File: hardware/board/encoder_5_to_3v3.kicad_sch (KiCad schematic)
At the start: 6 parts, among them U1 74LVCH2T45DC

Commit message: update schematic
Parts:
- renumbered C39 to C26, C19 to C27, C19 to C3, C9 to C4, U1 to U?
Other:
- note added: "B set to input."
- note added: "External Encoder Input"
- note removed: "Encoder Input"
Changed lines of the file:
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@@
     (stroke (width 0) (type default))
   )
-  (text "Encoder\nInput" (at 170.815 95.25 0)
+  (text "External\nEncoder\nInput" (at 170.815 97.155 0)
+    (effects (font (size 1.27 1.27)) (justify left bottom))
+  )
+  (text "B set to input." (at 116.84 103.505 0)
     (effects (font (size 1.27 1.27)) (justify left bottom))
   )
@@
   (symbol (lib_id "power:GND") (at 144.145 109.22 0) (unit 1)
     (in_bom yes) (on_board yes) (dnp no) (fields_autoplaced)
-    (property "Reference" "#PWR099" (at 144.145 115.57 0)
+    (property "Reference" "#PWR091" (at 144.145 115.57 0)
       (effects (font (size 1.27 1.27)) hide)
     )
@@
   (symbol (lib_id "Device:C") (at 168.275 182.245 180) (unit 1)
     (in_bom yes) (on_board yes) (dnp no)
-    (property "Reference" "C19" (at 172.085 179.705 0)
+    (property "Reference" "C27" (at 172.085 179.705 0)
       (effects (font (size 1.27 1.27)) (justify left))
     )
@@
   (symbol (lib_id "power:+5V") (at 168.275 177.165 0) (unit 1)
     (in_bom yes) (on_board yes) (dnp no)
-    (property "Reference" "#PWR0115" (at 168.275 180.975 0)
+    (property "Reference" "#PWR097" (at 168.275 180.975 0)
       (effects (font (size 1.27 1.27)) hide)
     )
@@
   (symbol (lib_id "Device:C") (at 136.525 182.245 180) (unit 1)
     (in_bom yes) (on_board yes) (dnp no)
-    (property "Reference" "C19" (at 140.335 179.705 0)
+    (property "Reference" "C3" (at 140.335 179.705 0)
       (effects (font (size 1.27 1.27)) (justify left))
     )
@@
   (symbol (lib_id "power:GND") (at 158.115 187.325 0) (unit 1)
     (in_bom yes) (on_board yes) (dnp no)
-    (property "Reference" "#PWR083" (at 158.115 193.675 0)
+    (property "Reference" "#PWR096" (at 158.115 193.675 0)
       (effects (font (size 1.27 1.27)) hide)
     )
@@
   (symbol (lib_id "power:GND") (at 168.275 187.325 0) (unit 1)
     (in_bom yes) (on_board yes) (dnp no)
-    (property "Reference" "#PWR0114" (at 168.275 193.675 0)
+    (property "Reference" "#PWR098" (at 168.275 193.675 0)
       (effects (font (size 1.27 1.27)) hide)
     )
@@
   (symbol (lib_id "Device:C") (at 144.78 182.245 0) (unit 1)
     (in_bom yes) (on_board yes) (dnp no)
-    (property "Reference" "C9" (at 146.05 179.705 0)
+    (property "Reference" "C4" (at 146.05 179.705 0)
       (effects (font (size 1.27 1.27)) (justify left))
     )
@@
   (symbol (lib_id "Logic_LevelTranslator:74LVCH2T45DC") (at 144.145 94.615 0) (unit 1)
     (in_bom yes) (on_board yes) (dnp no) (fields_autoplaced)
-    (property "Reference" "U1" (at 146.3391 106.68 0)
+    (property "Reference" "U?" (at 146.3391 106.68 0)
       (effects (font (size 1.27 1.27)) (justify left))
     )
@@
   (symbol (lib_id "power:GND") (at 144.78 187.325 0) (unit 1)
     (in_bom yes) (on_board yes) (dnp no)
-    (property "Reference" "#PWR081" (at 144.78 193.675 0)
+    (property "Reference" "#PWR093" (at 144.78 193.675 0)
       (effects (font (size 1.27 1.27)) hide)
     )
@@
   (symbol (lib_id "power:GND") (at 136.525 187.325 0) (unit 1)
     (in_bom yes) (on_board yes) (dnp no)
-    (property "Reference" "#PWR0113" (at 136.525 193.675 0)
+    (property "Reference" "#PWR089" (at 136.525 193.675 0)
       (effects (font (size 1.27 1.27)) hide)
     )
@@
   (symbol (lib_id "power:+5V") (at 158.115 177.165 0) (unit 1)
     (in_bom yes) (on_board yes) (dnp no)
-    (property "Reference" "#PWR082" (at 158.115 180.975 0)
+    (property "Reference" "#PWR095" (at 158.115 180.975 0)
       (effects (font (size 1.27 1.27)) hide)
     )
@@
   (symbol (lib_id "power:GND") (at 161.925 99.695 0) (unit 1)
     (in_bom yes) (on_board yes) (dnp no)
-    (property "Reference" "#PWR099" (at 161.925 106.045 0)
+    (property "Reference" "#PWR0100" (at 161.925 106.045 0)
       (effects (font (size 1.27 1.27)) hide)
     )
@@
   (symbol (lib_id "Device:C") (at 158.115 182.245 0) (unit 1)
     (in_bom yes) (on_board yes) (dnp no)
-    (property "Reference" "C39" (at 159.385 179.705 0)
-      (effects (font (size 1.27 1.27)) (justify left))
-    )
+    (property "Reference" "C26" (at 159.385 179.705 0)
+      (effects (font (size 1.27 1.27)) (justify left))
+    )

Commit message: update schematic
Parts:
- added C33: 1uF, Capacitor_SMD:C_0402_1005Metric, symbol Device:C
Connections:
- net +5V: now also C33.1
- net GND: now also C33.2
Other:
- note added: "BufferA Bypass Caps"
- note added: "Encoder/BufferB Bypass Caps"
- moved on the sheet: C3, C4

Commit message: update pcb
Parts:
- gave numbers to parts that had none: 2
- renumbered C3 to C53, C4 to C54, C33 to C55, C26 to C57, C27 to C58
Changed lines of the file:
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@@
   (symbol (lib_id "Device:C") (at 168.275 182.245 180) (unit 1)
     (in_bom yes) (on_board yes) (dnp no)
-    (property "Reference" "C27" (at 172.085 179.705 0)
+    (property "Reference" "C58" (at 172.085 179.705 0)
       (effects (font (size 1.27 1.27)) (justify left))
     )
@@
       (project "harp_treadmill"
         (path "/e63e39d7-6ac0-4ffd-8aa3-1841a4541b55/45528c19-905b-4605-ba1b-282fdcb272c9"
-          (reference "C27") (unit 1)
+          (reference "C58") (unit 1)
         )
       )
@@
   (symbol (lib_id "Device:C") (at 122.555 182.245 180) (unit 1)
     (in_bom yes) (on_board yes) (dnp no)
-    (property "Reference" "C3" (at 126.365 179.705 0)
+    (property "Reference" "C53" (at 126.365 179.705 0)
       (effects (font (size 1.27 1.27)) (justify left))
     )
@@
       (project "harp_treadmill"
         (path "/e63e39d7-6ac0-4ffd-8aa3-1841a4541b55/45528c19-905b-4605-ba1b-282fdcb272c9"
-          (reference "C3") (unit 1)
+          (reference "C53") (unit 1)
         )
       )
@@
   (symbol (lib_id "Connector:Conn_01x04_Female") (at 168.275 93.345 0) (unit 1)
     (in_bom yes) (on_board yes) (dnp no)
-    (property "Reference" "J?" (at 166.37 88.9 0)
+    (property "Reference" "J7" (at 166.37 88.9 0)
       (effects (font (size 1.27 1.27)) (justify left))
     )
@@
       (project "harp_treadmill"
         (path "/e63e39d7-6ac0-4ffd-8aa3-1841a4541b55/45528c19-905b-4605-ba1b-282fdcb272c9"
-          (reference "J?") (unit 1)
+          (reference "J7") (unit 1)
         )
       )
@@
   (symbol (lib_id "Device:C") (at 147.955 182.245 0) (unit 1)
     (in_bom yes) (on_board yes) (dnp no)
-    (property "Reference" "C33" (at 149.225 179.705 0)
+    (property "Reference" "C55" (at 149.225 179.705 0)
       (effects (font (size 1.27 1.27)) (justify left))
     )
@@
       (project "harp_treadmill"
         (path "/e63e39d7-6ac0-4ffd-8aa3-1841a4541b55/45528c19-905b-4605-ba1b-282fdcb272c9"
-          (reference "C33") (unit 1)
+          (reference "C55") (unit 1)
         )
       )
@@
   (symbol (lib_id "Device:C") (at 130.81 182.245 0) (unit 1)
     (in_bom yes) (on_board yes) (dnp no)
-    (property "Reference" "C4" (at 132.08 179.705 0)
+    (property "Reference" "C54" (at 132.08 179.705 0)
       (effects (font (size 1.27 1.27)) (justify left))
     )
@@
       (project "harp_treadmill"
         (path "/e63e39d7-6ac0-4ffd-8aa3-1841a4541b55/45528c19-905b-4605-ba1b-282fdcb272c9"
-          (reference "C4") (unit 1)
+          (reference "C54") (unit 1)
         )
       )
@@
   (symbol (lib_id "Logic_LevelTranslator:74LVCH2T45DC") (at 144.145 94.615 0) (unit 1)
     (in_bom yes) (on_board yes) (dnp no) (fields_autoplaced)
-    (property "Reference" "U?" (at 146.3391 106.68 0)
+    (property "Reference" "U15" (at 146.3391 106.68 0)
       (effects (font (size 1.27 1.27)) (justify left))
     )
@@
       (project "harp_treadmill"
         (path "/e63e39d7-6ac0-4ffd-8aa3-1841a4541b55/45528c19-905b-4605-ba1b-282fdcb272c9"
-          (reference "U?") (unit 1)
+          (reference "U15") (unit 1)
         )
       )
@@
   (symbol (lib_id "Device:C") (at 158.115 182.245 0) (unit 1)
     (in_bom yes) (on_board yes) (dnp no)
-    (property "Reference" "C26" (at 159.385 179.705 0)
+    (property "Reference" "C57" (at 159.385 179.705 0)
       (effects (font (size 1.27 1.27)) (justify left))
     )
@@
       (project "harp_treadmill"
         (path "/e63e39d7-6ac0-4ffd-8aa3-1841a4541b55/45528c19-905b-4605-ba1b-282fdcb272c9"
-          (reference "C26") (unit 1)
-        )
-      )
+          (reference "C57") (unit 1)
+        )
+      )

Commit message: update sch and pcb
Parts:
- C57: Alternate CL21B106KOQNNNE -> GRM21BR61H106KE43L; Link https://www.digikey.com/en/products/detail/murata-electronics/GRM21BZ71E106KE15L/13904911 -> https://www.digikey.com/en/products/detail/murata-electronics/GRM21BR61H106KE43L/10326316; Manufacturer Number GRM21BZ71E106KE15L -> GRM21BR61H106KE43L; Rated Voltage 25V -> 50V; Temperature Coefficient X7R -> X5R; Tolerance (none) -> 10%
- J7: footprint (none) -> Connector_Phoenix_MC:PhoenixContact_MC_1,5_4-G-3.5_1x04_P3.50mm_Horizontal; Link (none) -> https://www.digikey.com/en/products/detail/phoenix-contact/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; Manufacturer (none) -> Phoenix Contact; Manufacturer Number (none) -> 1844236
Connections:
- net ENC_A: now also U15.3 (2A); no longer U15.2 (1A)
- net ENC_B: now also U15.2 (1A); no longer U15.3 (2A)
- net at J7.2 (Pin_2): now also U15.6 (2B); no longer U15.7 (1B)
- net at J7.3 (Pin_3): now also U15.7 (1B); no longer U15.6 (2B)
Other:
- note added: "Mates with: 1862878"

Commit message: update schematic; continue pcb draft
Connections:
- net +5V renamed 5V2
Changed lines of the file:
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@@
     (stroke (width 0) (type default))
   )
-  (wire (pts (xy 147.955 177.165) (xy 147.955 178.435))
+  (wire (pts (xy 147.955 175.26) (xy 147.955 178.435))
     (stroke (width 0) (type default))
   )
@@
     (stroke (width 0) (type default))
   )
-  (wire (pts (xy 168.275 177.165) (xy 168.275 178.435))
+  (wire (pts (xy 168.275 175.26) (xy 168.275 178.435))
     (stroke (width 0) (type default))
   )
@@
     (stroke (width 0) (type default))
   )
-  (wire (pts (xy 162.052 89.154) (xy 162.052 90.424))
+  (wire (pts (xy 162.052 85.09) (xy 162.052 90.424))
     (stroke (width 0) (type default))
   )
@@
     (stroke (width 0) (type default))
   )
-  (wire (pts (xy 158.115 177.165) (xy 158.115 178.435))
+  (wire (pts (xy 158.115 175.26) (xy 158.115 178.435))
     (stroke (width 0) (type default))
   )
@@
   (text "BufferA\nBypass Caps" (at 119.38 169.545 0)
     (effects (font (size 1.27 1.27)) (justify left bottom))
+  )
+  (global_label "5V2" (shape input) (at 162.052 85.09 0) (fields_autoplaced)
+    (effects (font (size 1.27 1.27)) (justify left))
+    (property "Intersheetrefs" "${INTERSHEET_REFS}" (at 168.5448 85.09 0)
+      (effects (font (size 1.27 1.27)) (justify left) hide)
+    )
+  )
+  (global_label "5V2" (shape input) (at 146.812 80.264 0) (fields_autoplaced)
+    (effects (font (size 1.27 1.27)) (justify left))
+    (property "Intersheetrefs" "${INTERSHEET_REFS}" (at 153.3048 80.264 0)
+      (effects (font (size 1.27 1.27)) (justify left) hide)
+    )
+  )
+  (global_label "5V2" (shape input) (at 147.955 175.26 180) (fields_autoplaced)
+    (effects (font (size 1.27 1.27)) (justify right))
+    (property "Intersheetrefs" "${INTERSHEET_REFS}" (at 141.4622 175.26 0)
+      (effects (font (size 1.27 1.27)) (justify right) hide)
+    )
+  )
+  (global_label "5V2" (shape input) (at 168.275 175.26 180) (fields_autoplaced)
+    (effects (font (size 1.27 1.27)) (justify right))
+    (property "Intersheetrefs" "${INTERSHEET_REFS}" (at 161.7822 175.26 0)
+      (effects (font (size 1.27 1.27)) (justify right) hide)
+    )
+  )
+  (global_label "5V2" (shape input) (at 158.115 175.26 180) (fields_autoplaced)
+    (effects (font (size 1.27 1.27)) (justify right))
+    (property "Intersheetrefs" "${INTERSHEET_REFS}" (at 151.6222 175.26 0)
+      (effects (font (size 1.27 1.27)) (justify right) hide)
+    )
   )
   (hierarchical_label "ENC_B" (shape input) (at 132.842 91.694 180) (fields_autoplaced)
@@
         (path "/e63e39d7-6ac0-4ffd-8aa3-1841a4541b55/45528c19-905b-4605-ba1b-282fdcb272c9"
           (reference "#PWR088") (unit 1)
-        )
-      )
-    )
-  )
-  (symbol (lib_id "power:+5V") (at 168.275 177.165 0) (unit 1)
-    (in_bom yes) (on_board yes) (dnp no)
-    (property "Reference" "#PWR097" (at 168.275 180.975 0)
-      (effects (font (size 1.27 1.27)) hide)
-    )
-    (property "Value" "+5V" (at 168.275 173.355 0)
-      (effects (font (size 1.27 1.27)))
-    )
-    (property "Footprint" "" (at 168.275 177.165 0)
-      (effects (font (size 1.27 1.27)) hide)
-    )
-    (property "Datasheet" "" (at 168.275 177.165 0)
-      (effects (font (size 1.27 1.27)) hide)
-    )
-    (pin "1")
-    (instances
-      (project "harp_treadmill"
-        (path "/e63e39d7-6ac0-4ffd-8aa3-1841a4541b55/45528c19-905b-4605-ba1b-282fdcb272c9"
-          (reference "#PWR097") (unit 1)
         )
       )
@@
     )
   )
-  (symbol (lib_id "power:+5V") (at 147.955 177.165 0) (unit 1)
-    (in_bom yes) (on_board yes) (dnp no)
-    (property "Reference" "#PWR0114" (at 147.955 180.975 0)
-      (effects (font (size 1.27 1.27)) hide)
-    )
-    (property "Value" "+5V" (at 147.955 173.355 0)
-      (effects (font (size 1.27 1.27)))
-    )
-    (property "Footprint" "" (at 147.955 177.165 0)
-      (effects (font (size 1.27 1.27)) hide)
-    )
-    (property "Datasheet" "" (at 147.955 177.165 0)
-      (effects (font (size 1.27 1.27)) hide)
-    )
-    (pin "1")
-    (instances
-      (project "harp_treadmill"
-        (path "/e63e39d7-6ac0-4ffd-8aa3-1841a4541b55/45528c19-905b-4605-ba1b-282fdcb272c9"
-          (reference "#PWR0114") (unit 1)
-        )
-      )
-    )
-  )
   (symbol (lib_id "power:GND") (at 130.81 187.325 0) (unit 1)
     (in_bom yes) (on_board yes) (dnp no)
@@
     )
   )
-  (symbol (lib_id "power:+5V") (at 158.115 177.165 0) (unit 1)
-    (in_bom yes) (on_board yes) (dnp no)
-    (property "Reference" "#PWR095" (at 158.115 180.975 0)
-      (effects (font (size 1.27 1.27)) hide)
-    )
-    (property "Value" "+5V" (at 158.115 173.355 0)
-      (effects (font (size 1.27 1.27)))
-    )
-    (property "Footprint" "" (at 158.115 177.165 0)
-      (effects (font (size 1.27 1.27)) hide)
-    )
-    (property "Datasheet" "" (at 158.115 177.165 0)
-      (effects (font (size 1.27 1.27)) hide)
-    )
-    (pin "1")
-    (instances
-      (project "harp_treadmill"
-        (path "/e63e39d7-6ac0-4ffd-8aa3-1841a4541b55/45528c19-905b-4605-ba1b-282fdcb272c9"
-          (reference "#PWR095") (unit 1)
-        )
-      )
-    )
-  )
   (symbol (lib_id "power:GND") (at 147.955 187.325 0) (unit 1)
     (in_bom yes) (on_board yes) (dnp no)
@@
     )
   )
-  (symbol (lib_id "power:+5V") (at 146.812 80.264 0) (unit 1)
-    (in_bom yes) (on_board yes) (dnp no)
-    (property "Reference" "#PWR0105" (at 146.812 84.074 0)
-      (effects (font (size 1.27 1.27)) hide)
-    )
-    (property "Value" "+5V" (at 146.812 76.454 0)
-      (effects (font (size 1.27 1.27)))
-    )
-    (property "Footprint" "" (at 146.812 80.264 0)
-      (effects (font (size 1.27 1.27)) hide)
-    )
-    (property "Datasheet" "" (at 146.812 80.264 0)
-      (effects (font (size 1.27 1.27)) hide)
-    )
-    (pin "1")
-    (instances
-      (project "harp_treadmill"
-        (path "/e63e39d7-6ac0-4ffd-8aa3-1841a4541b55"
-          (reference "#PWR0105") (unit 1)
-        )
-        (path "/e63e39d7-6ac0-4ffd-8aa3-1841a4541b55/45528c19-905b-4605-ba1b-282fdcb272c9"
-          (reference "#PWR094") (unit 1)
-        )
-      )
-    )
-  )
   (symbol (lib_id "power:GND") (at 162.052 99.314 0) (unit 1)
     (in_bom yes) (on_board yes) (dnp no)
@@
         )
       )
-    )
-  )
-  (symbol (lib_id "power:+5V") (at 162.052 89.154 0) (unit 1)
-    (in_bom yes) (on_board yes) (dnp no)
-    (property "Reference" "#PWR0105" (at 162.052 92.964 0)
-      (effects (font (size 1.27 1.27)) hide)
-    )
-    (property "Value" "+5V" (at 162.052 85.344 0)
-      (effects (font (size 1.27 1.27)))
-    )
-    (property "Footprint" "" (at 162.052 89.154 0)
-      (effects (font (size 1.27 1.27)) hide)
-    )
-    (property "Datasheet" "" (at 162.052 89.154 0)
-      (effects (font (size 1.27 1.27)) hide)
-    )
-    (pin "1")
-    (instances
-      (project "harp_treadmill"
-        (path "/e63e39d7-6ac0-4ffd-8aa3-1841a4541b55"
-          (reference "#PWR0105") (unit 1)
-        )
-        (path "/e63e39d7-6ac0-4ffd-8aa3-1841a4541b55/45528c19-905b-4605-ba1b-282fdcb272c9"
-          (reference "#PWR087") (unit 1)
-        )
-      )

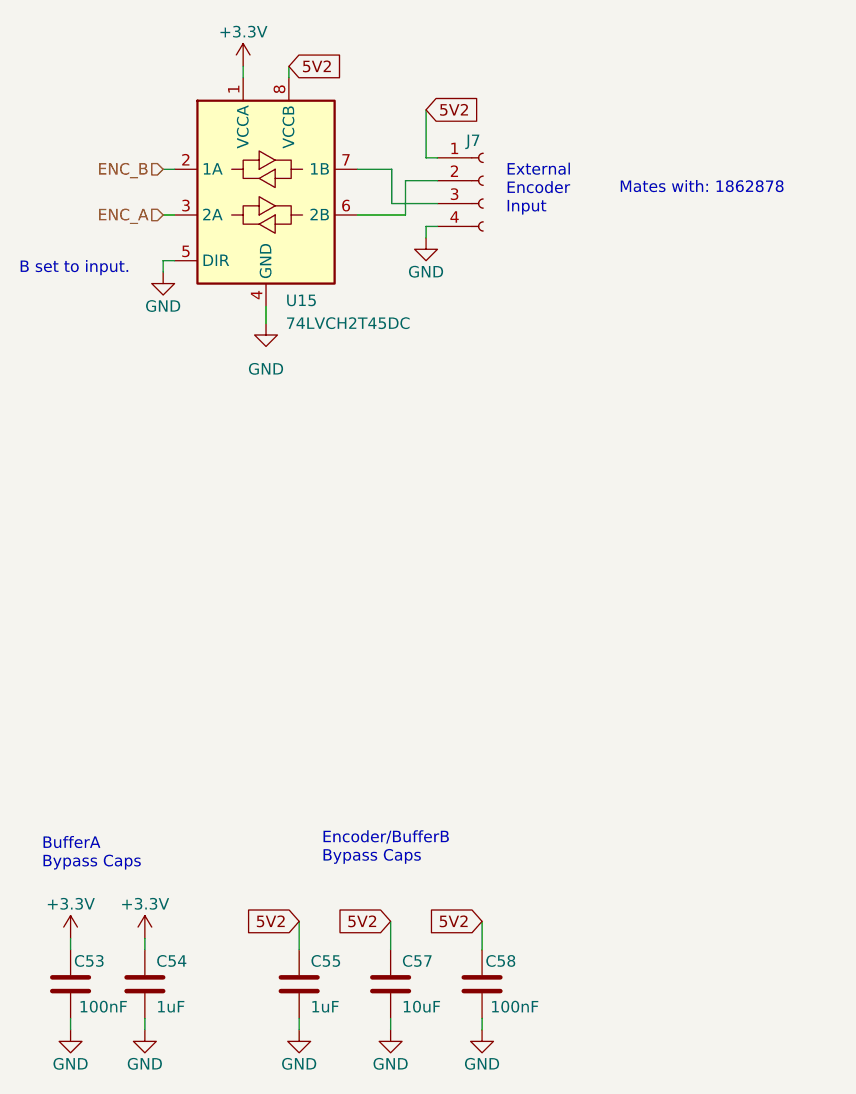
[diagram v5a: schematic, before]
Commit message: draft layout with analog brake driver circuit
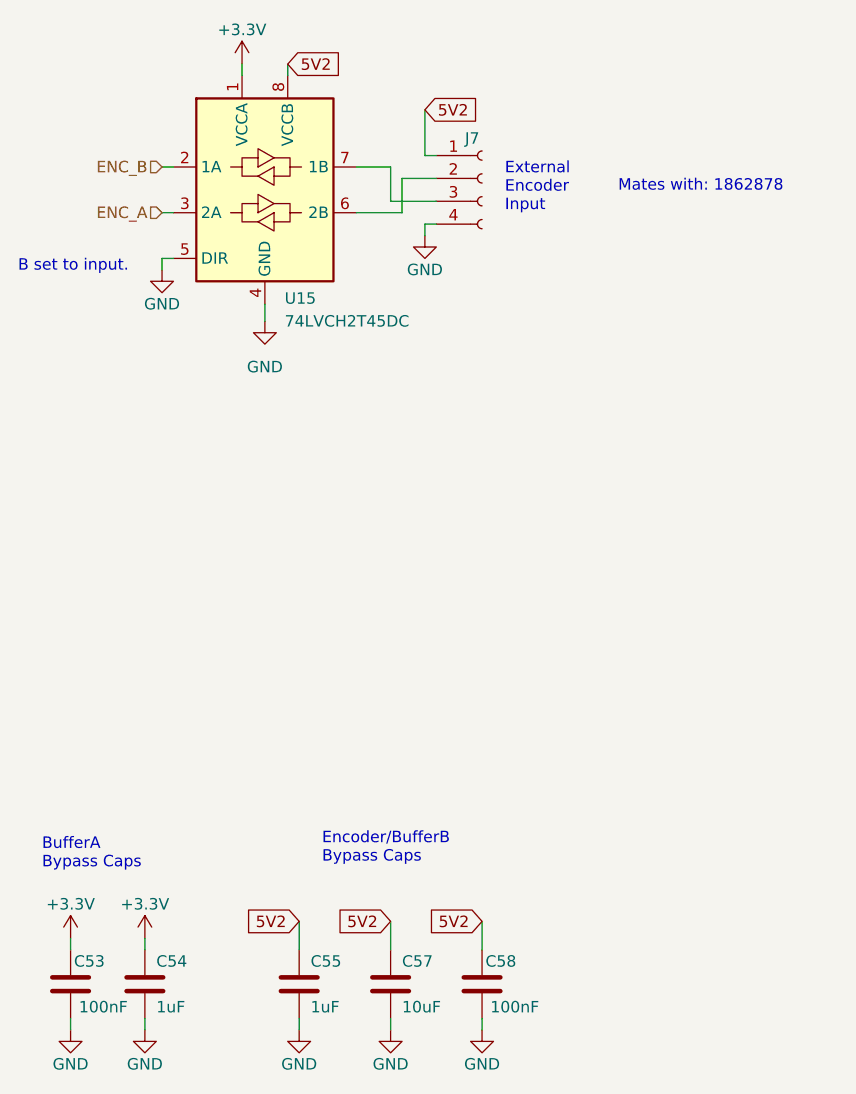
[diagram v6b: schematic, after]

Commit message: update silkscreen size; add mating connector note
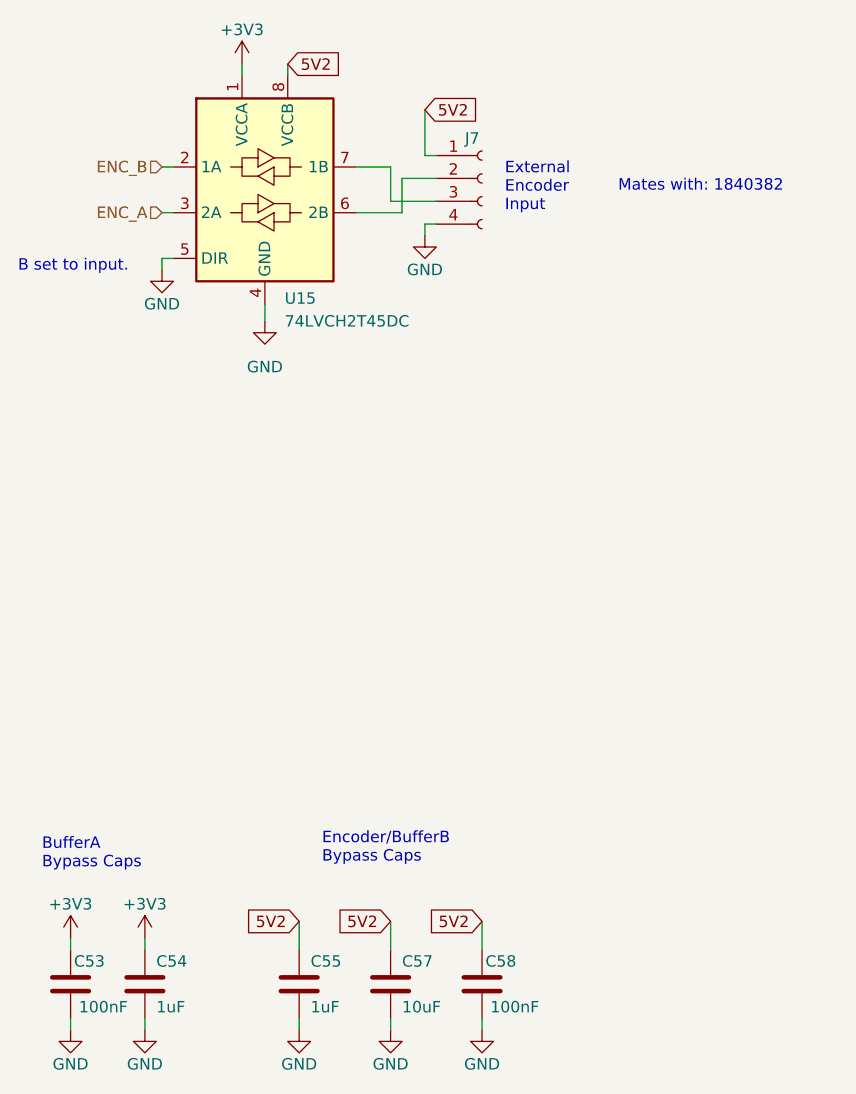
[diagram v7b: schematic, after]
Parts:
- J7: Notes (none) -> mates with 1840382
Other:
- note added: "Mates with: 1840382"
- note removed: "Mates with: 1862878"
